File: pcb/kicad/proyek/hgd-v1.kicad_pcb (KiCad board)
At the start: 2 copper layers, 80 x 55 mm, 18 parts, among them J1 HX711 01x04_Socket, J2 LCD I2C 01x04_Socket, J3 LV Conn_01x06_Socket, J4 HV Conn_01x06_Socket, SW1 SW_Push, U2 ESP32-DEVKIT-V1

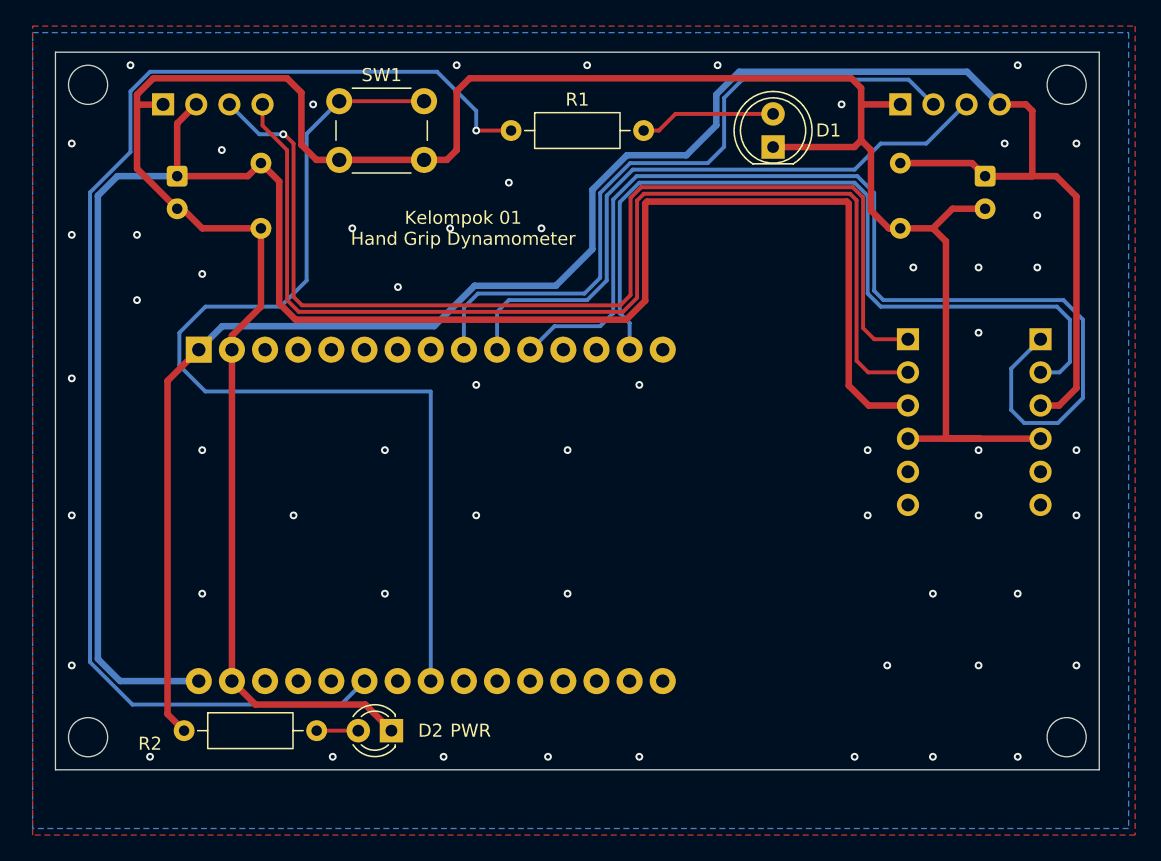
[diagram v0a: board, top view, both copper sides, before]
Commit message: PCB: versi akhir 26 Okt. 2026 (skema, papan, PDF skema, tangkapan)
- hgd-v1.kicad_sch: judul "Digital Hand Grip Dynamometer" (hanya title block).
- hgd-v1.kicad_pcb: jalur ulang dengan posisi footprint tetap (56 via GND),
  silkscreen tiga baris, stackup FR4 1,6 mm; folder keluaran Gerber kembali
  ke gerber/ (tanpa jalur lokal).
- hgd-v1.kicad_pro baru (jalur keluaran relatif di dalam proyek).
- PDF skema, tangkapan Assign Footprints, ERC, DRC, dan render papan/3D.
- Desain PCB v8 (Bagian 8.1a daftar Assign Footprints), log kerja KiCad v2,
  README KiCad v6, catatan proyek v59.
- Gambar penempatan, salinan verbatim, dan STEP tetap versi 17 Okt.;
  Gerber tetap di luar repo sampai disetujui.

Co-Authored-By: Claude Opus 5.5 <noreply@anthropic.com>
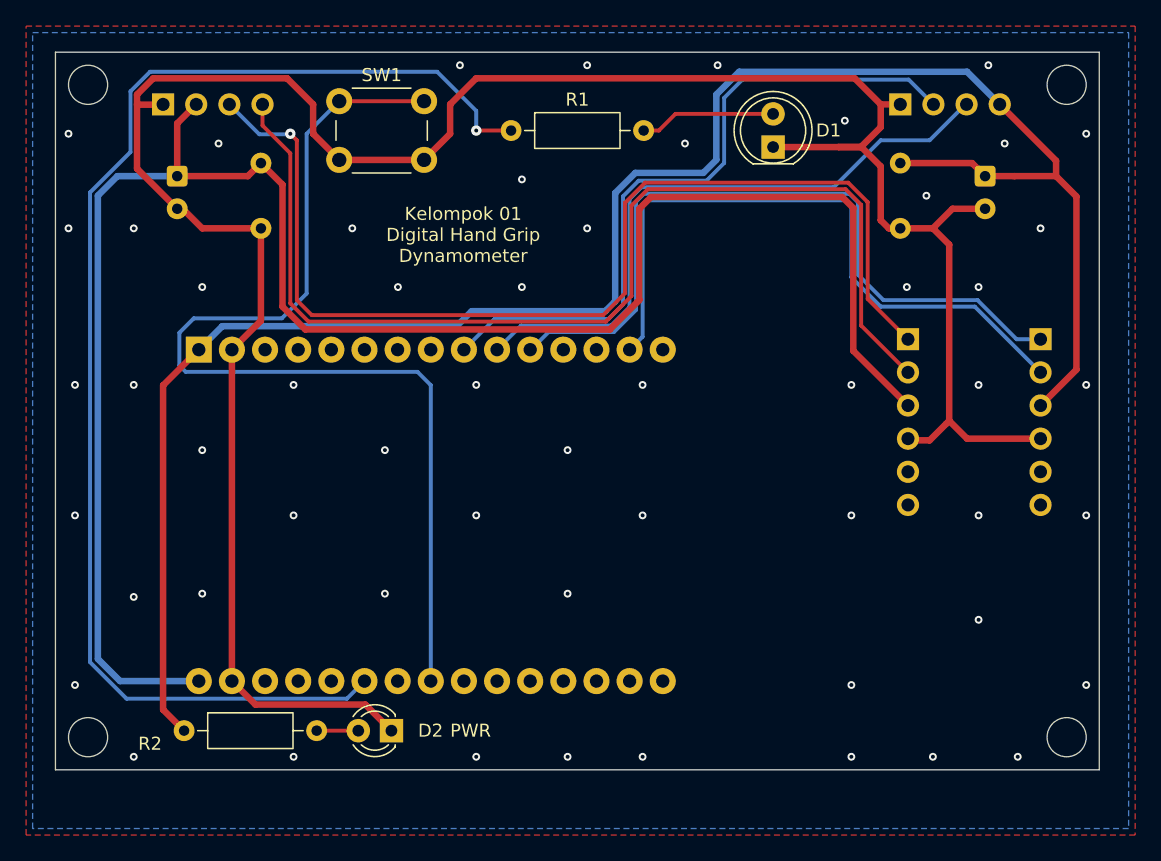
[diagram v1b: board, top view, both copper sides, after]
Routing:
- net Net-(J3-LV1): track 81.0 -> 56.8 mm
- net Net-(J3-LV2): track 61.3 -> 50.9 mm
- net GND: track 193.9 -> 189.3 mm, vias 57 -> 56
- net Net-(J2-SCL): track 84.7 -> 83.6 mm
- net Net-(J2-VCC): track 146.4 -> 145.3 mm
- net Net-(U2-D25): track 77.5 -> 78.4 mm
- net Net-(J1-VCC): track 149.9 -> 149.0 mm
- net Net-(J1-SCK): track 49.2 -> 48.6 mm
- net Net-(J2-SDA): track 84.1 -> 83.5 mm
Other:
- board text added: "Kelompok 01 Digital Hand Grip Dynamometer"
- board text removed: "Kelompok 01 Hand Grip Dynamometer"
